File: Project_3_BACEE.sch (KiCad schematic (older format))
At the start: 13 parts, among them U1 DS1337, U2 24LC1025, U3 24LC1025, U4 ATMEGA328P-AU, Y1 Crystal, Y2 Crystal

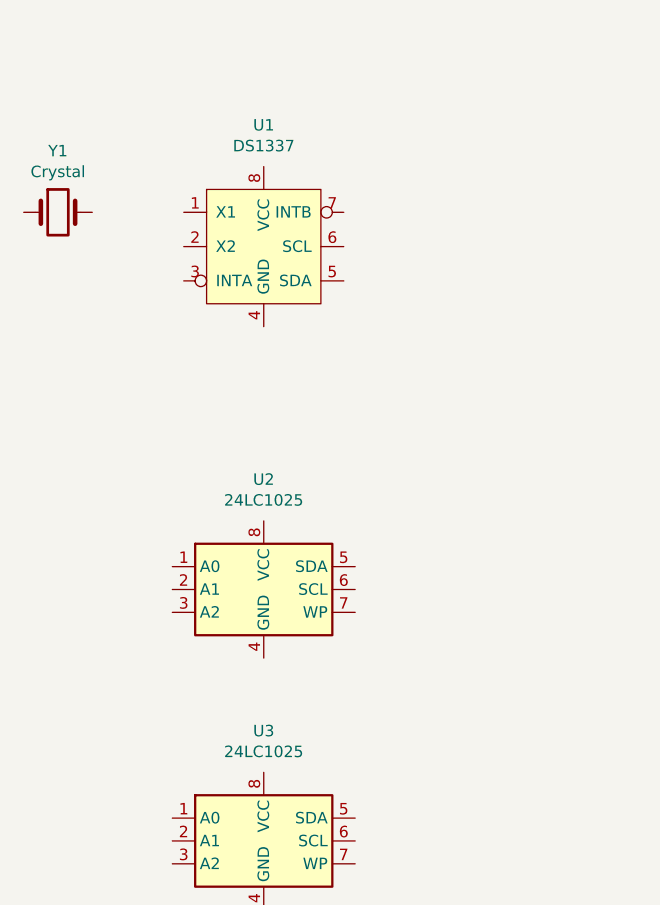
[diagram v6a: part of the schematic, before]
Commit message: Added footprints assigments.
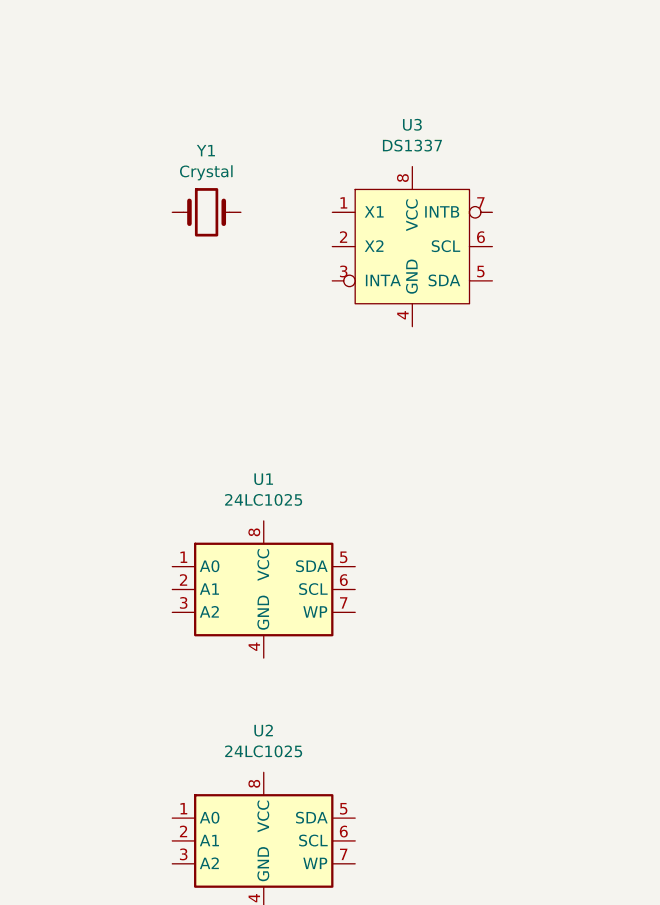
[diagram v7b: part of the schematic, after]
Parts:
- BT1: footprint (none) -> Connector_PinHeader_2.54mm:PinHeader_1x02_P2.54mm_Vertical
- C1, C2, C3: footprint (none) -> Capacitor_SMD:C_0805_2012Metric_Pad1.15x1.40mm_HandSolder
- D1: footprint (none) -> LED_SMD:LED_0805_2012Metric_Pad1.15x1.40mm_HandSolder
- R1, R2: footprint (none) -> Resistor_SMD:R_0805_2012Metric_Pad1.15x1.40mm_HandSolder
- U1: renamed from U2; footprint (none) -> Package_SO:SOIJ-8_5.3x5.3mm_P1.27mm
- U2: renamed from U3; footprint (none) -> Package_SO:SOIJ-8_5.3x5.3mm_P1.27mm
- U3: renamed from U1; footprint (none) -> Package_SO:SO-8_5.3x6.2mm_P1.27mm
- Y1: footprint (none) -> Crystal:Crystal_SMD_MicroCrystal_CC7V-T1A-2Pin_3.2x1.5mm_HandSoldering
- Y2: footprint (none) -> Crystal:Crystal_SMD_5032-2Pin_5.0x3.2mm_HandSoldering
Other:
- moved on the sheet: U3, Y1
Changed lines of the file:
@@
 F 0 "BT1" H 10258 1846 50  0000 L CNN
 F 1 "Battery" H 10258 1755 50  0000 L CNN
-F 2 "" V 10150 1860 50  0001 C CNN
+F 2 "Connector_PinHeader_2.54mm:PinHeader_1x02_P2.54mm_Vertical" V 10150 1860 50  0001 C CNN
 F 3 "~" V 10150 1860 50  0001 C CNN
 	1    10150 1800
@@
 F 0 "C1" H 5215 2696 50  0000 L CNN
 F 1 "C" H 5215 2605 50  0000 L CNN
-F 2 "" H 5138 2500 50  0001 C CNN
+F 2 "Capacitor_SMD:C_0805_2012Metric_Pad1.15x1.40mm_HandSolder" H 5138 2500 50  0001 C CNN
 F 3 "~" H 5100 2650 50  0001 C CNN
 	1    5100 2650
@@
 F 0 "C2" H 5215 3096 50  0000 L CNN
 F 1 "C" H 5215 3005 50  0000 L CNN
-F 2 "" H 5138 2900 50  0001 C CNN
+F 2 "Capacitor_SMD:C_0805_2012Metric_Pad1.15x1.40mm_HandSolder" H 5138 2900 50  0001 C CNN
 F 3 "~" H 5100 3050 50  0001 C CNN
 	1    5100 3050
@@
 F 0 "C3" H 10568 2446 50  0000 L CNN
 F 1 "CP" H 10568 2355 50  0000 L CNN
-F 2 "" H 10488 2250 50  0001 C CNN
+F 2 "Capacitor_SMD:C_0805_2012Metric_Pad1.15x1.40mm_HandSolder" H 10488 2250 50  0001 C CNN
 F 3 "~" H 10450 2400 50  0001 C CNN
 	1    10450 2400
@@
 F 0 "D1" V 4439 4483 50  0000 R CNN
 F 1 "LED" V 4348 4483 50  0000 R CNN
-F 2 "" H 4400 4600 50  0001 C CNN
+F 2 "LED_SMD:LED_0805_2012Metric_Pad1.15x1.40mm_HandSolder" H 4400 4600 50  0001 C CNN
 F 3 "~" H 4400 4600 50  0001 C CNN
 	1    4400 4600
@@
 F 0 "R1" H 4420 2646 50  0000 L CNN
 F 1 "R" H 4420 2555 50  0000 L CNN
-F 2 "" V 4280 2600 50  0001 C CNN
+F 2 "Resistor_SMD:R_0805_2012Metric_Pad1.15x1.40mm_HandSolder" V 4280 2600 50  0001 C CNN
 F 3 "~" H 4350 2600 50  0001 C CNN
 	1    4350 2600
@@
 F 0 "R2" H 4470 4046 50  0000 L CNN
 F 1 "R" H 4470 3955 50  0000 L CNN
-F 2 "" V 4330 4000 50  0001 C CNN
+F 2 "Resistor_SMD:R_0805_2012Metric_Pad1.15x1.40mm_HandSolder" V 4330 4000 50  0001 C CNN
 F 3 "~" H 4400 4000 50  0001 C CNN
 	1    4400 4000
@@
 $EndComp
 $Comp
-L Memory_EEPROM:24LC1025 U2
+L Memory_EEPROM:24LC1025 U1
 U 1 1 5D83A291
 P 2000 4100
-F 0 "U2" H 2000 4581 50  0000 C CNN
+F 0 "U1" H 2000 4581 50  0000 C CNN
 F 1 "24LC1025" H 2000 4490 50  0000 C CNN
-F 2 "" H 2000 4100 50  0001 C CNN
+F 2 "Package_SO:SOIJ-8_5.3x5.3mm_P1.27mm" H 2000 4100 50  0001 C CNN
 F 3 "http://ww1.microchip.com/downloads/en/DeviceDoc/21941B.pdf" H 2000 4100 50  0001 C CNN
 	1    2000 4100
@@
 $EndComp
 $Comp
-L Real_Time_Clock:DS1337 U1
+L Real_Time_Clock:DS1337 U3
 U 1 1 5D83D55D
-P 2000 2600
-F 0 "U1" H 2000 3131 50  0000 C CNN
-F 1 "DS1337" H 2000 3040 50  0000 C CNN
-F 2 "" H 2250 3350 50  0001 C CNN
-F 3 "http://www.farnell.com/datasheets/2000844.pdf?_ga=2.177508589.917776798.1568905288-909876714.1550950510&_gac=1.216414692.1568905288.Cj0KCQjwzozsBRCNARIsAEM9kBOgoySVZbm8O6iFhnJvaEFTPgnKihPjdqZAtUZmWq1n3gbdbDGyVXUaAgFCEALw_wcB" H 2250 3350 50  0001 C CNN
-	1    2000 2600
+P 2650 2600
+F 0 "U3" H 2650 3131 50  0000 C CNN
+F 1 "DS1337" H 2650 3040 50  0000 C CNN
+F 2 "Package_SO:SO-8_5.3x6.2mm_P1.27mm" H 2900 3350 50  0001 C CNN
+F 3 "http://www.farnell.com/datasheets/2000844.pdf?_ga=2.177508589.917776798.1568905288-909876714.1550950510&_gac=1.216414692.1568905288.Cj0KCQjwzozsBRCNARIsAEM9kBOgoySVZbm8O6iFhnJvaEFTPgnKihPjdqZAtUZmWq1n3gbdbDGyVXUaAgFCEALw_wcB" H 2900 3350 50  0001 C CNN
+	1    2650 2600
 	1    0    0    -1
 $EndComp
@@
 L Device:Crystal Y1
 U 1 1 5D83E063
-P 1100 2450
-F 0 "Y1" H 1100 2718 50  0000 C CNN
-F 1 "Crystal" H 1100 2627 50  0000 C CNN
-F 2 "" H 1100 2450 50  0001 C CNN
-F 3 "~" H 1100 2450 50  0001 C CNN
-	1    1100 2450
+P 1750 2450
+F 0 "Y1" H 1750 2718 50  0000 C CNN
+F 1 "Crystal" H 1750 2627 50  0000 C CNN
+F 2 "Crystal:Crystal_SMD_MicroCrystal_CC7V-T1A-2Pin_3.2x1.5mm_HandSoldering" H 1750 2450 50  0001 C CNN
+F 3 "~" H 1750 2450 50  0001 C CNN
+	1    1750 2450
 	1    0    0    -1
 $EndComp
@@
 F 0 "Y2" H 4750 3068 50  0000 C CNN
 F 1 "Crystal" H 4750 2977 50  0000 C CNN
-F 2 "" H 4750 2800 50  0001 C CNN
+F 2 "Crystal:Crystal_SMD_5032-2Pin_5.0x3.2mm_HandSoldering" H 4750 2800 50  0001 C CNN
 F 3 "~" H 4750 2800 50  0001 C CNN
 	1    4750 2800
@@
 $EndComp
 $Comp
-L Memory_EEPROM:24LC1025 U3
+L Memory_EEPROM:24LC1025 U2
 U 1 1 5D841166
 P 2000 5200
-F 0 "U3" H 2000 5681 50  0000 C CNN
+F 0 "U2" H 2000 5681 50  0000 C CNN
 F 1 "24LC1025" H 2000 5590 50  0000 C CNN
-F 2 "" H 2000 5200 50  0001 C CNN
+F 2 "Package_SO:SOIJ-8_5.3x5.3mm_P1.27mm" H 2000 5200 50  0001 C CNN
 F 3 "http://ww1.microchip.com/downloads/en/DeviceDoc/21941B.pdf" H 2000 5200 50  0001 C CNN
 	1    2000 5200

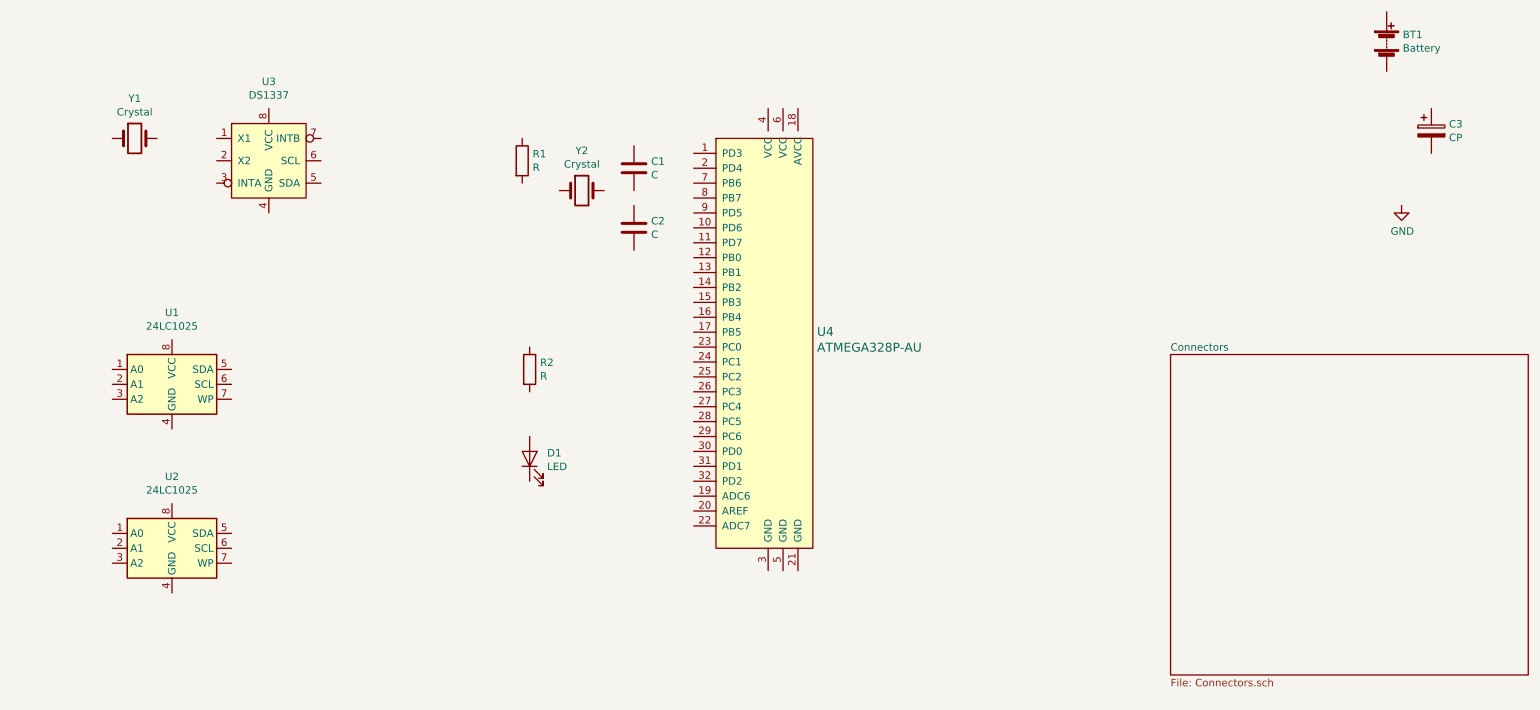
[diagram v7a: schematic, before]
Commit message: Completed asociations and added component values.
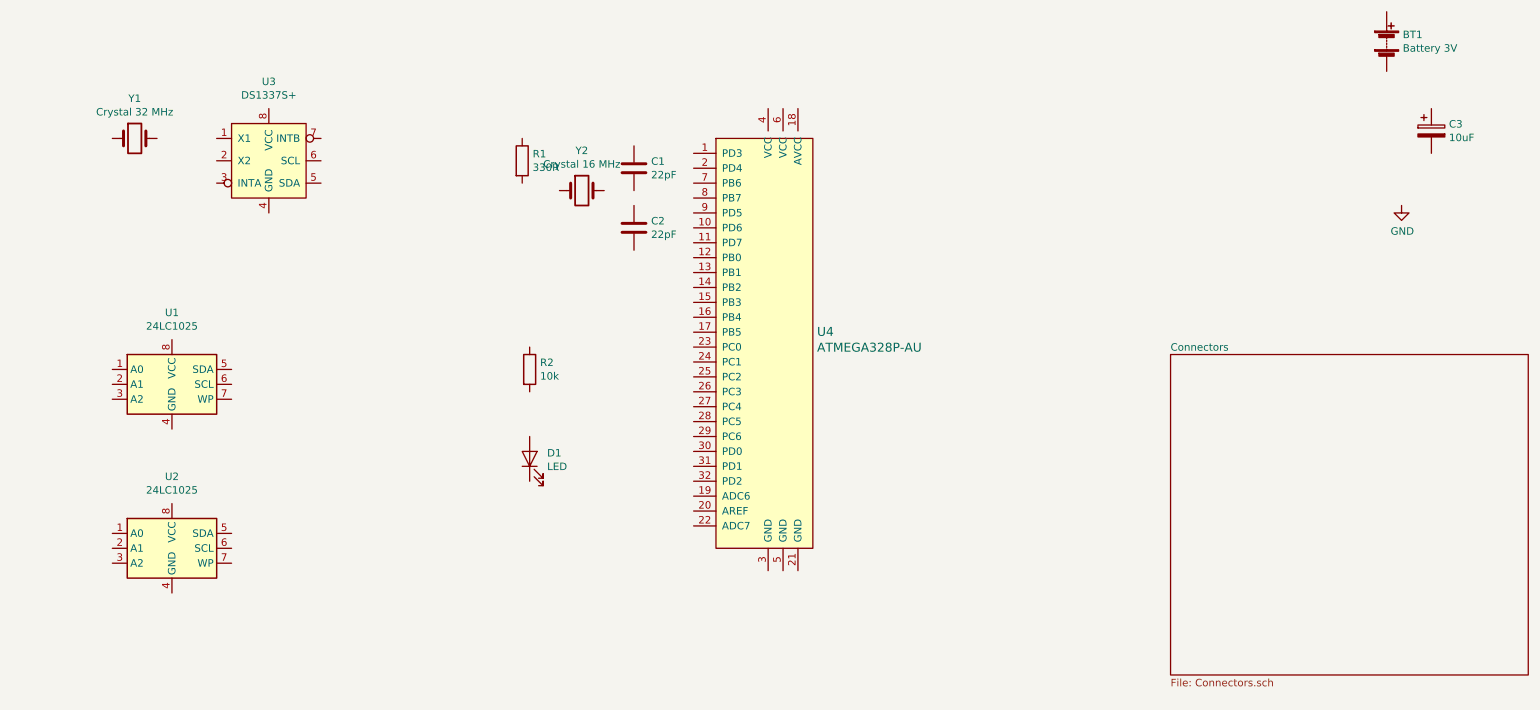
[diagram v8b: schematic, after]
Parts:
- BT1: value Battery -> Battery 3V
- C1, C2: value C -> 22pF
- C3: value CP -> 10uF
- R1: value R -> 330R
- R2: value R -> 10k
- U3: value DS1337 -> DS1337S+
- Y1: value Crystal -> Crystal 32 MHz
- Y2: value Crystal -> Crystal 16 MHz
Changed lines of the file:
@@
 P 10150 1800
 F 0 "BT1" H 10258 1846 50  0000 L CNN
-F 1 "Battery" H 10258 1755 50  0000 L CNN
+F 1 "Battery 3V" H 10258 1755 50  0000 L CNN
 F 2 "Connector_PinHeader_2.54mm:PinHeader_1x02_P2.54mm_Vertical" V 10150 1860 50  0001 C CNN
 F 3 "~" V 10150 1860 50  0001 C CNN
@@
 P 5100 2650
 F 0 "C1" H 5215 2696 50  0000 L CNN
-F 1 "C" H 5215 2605 50  0000 L CNN
+F 1 "22pF" H 5215 2605 50  0000 L CNN
 F 2 "Capacitor_SMD:C_0805_2012Metric_Pad1.15x1.40mm_HandSolder" H 5138 2500 50  0001 C CNN
 F 3 "~" H 5100 2650 50  0001 C CNN
@@
 P 5100 3050
 F 0 "C2" H 5215 3096 50  0000 L CNN
-F 1 "C" H 5215 3005 50  0000 L CNN
+F 1 "22pF" H 5215 3005 50  0000 L CNN
 F 2 "Capacitor_SMD:C_0805_2012Metric_Pad1.15x1.40mm_HandSolder" H 5138 2900 50  0001 C CNN
 F 3 "~" H 5100 3050 50  0001 C CNN
@@
 P 10450 2400
 F 0 "C3" H 10568 2446 50  0000 L CNN
-F 1 "CP" H 10568 2355 50  0000 L CNN
+F 1 "10uF" H 10568 2355 50  0000 L CNN
 F 2 "Capacitor_SMD:C_0805_2012Metric_Pad1.15x1.40mm_HandSolder" H 10488 2250 50  0001 C CNN
 F 3 "~" H 10450 2400 50  0001 C CNN
@@
 P 4350 2600
 F 0 "R1" H 4420 2646 50  0000 L CNN
-F 1 "R" H 4420 2555 50  0000 L CNN
+F 1 "330R" H 4420 2555 50  0000 L CNN
 F 2 "Resistor_SMD:R_0805_2012Metric_Pad1.15x1.40mm_HandSolder" V 4280 2600 50  0001 C CNN
 F 3 "~" H 4350 2600 50  0001 C CNN
@@
 P 4400 4000
 F 0 "R2" H 4470 4046 50  0000 L CNN
-F 1 "R" H 4470 3955 50  0000 L CNN
+F 1 "10k" H 4470 3955 50  0000 L CNN
 F 2 "Resistor_SMD:R_0805_2012Metric_Pad1.15x1.40mm_HandSolder" V 4330 4000 50  0001 C CNN
 F 3 "~" H 4400 4000 50  0001 C CNN
@@
 P 2650 2600
 F 0 "U3" H 2650 3131 50  0000 C CNN
-F 1 "DS1337" H 2650 3040 50  0000 C CNN
+F 1 "DS1337S+" H 2650 3040 50  0000 C CNN
 F 2 "Package_SO:SO-8_5.3x6.2mm_P1.27mm" H 2900 3350 50  0001 C CNN
 F 3 "http://www.farnell.com/datasheets/2000844.pdf?_ga=2.177508589.917776798.1568905288-909876714.1550950510&_gac=1.216414692.1568905288.Cj0KCQjwzozsBRCNARIsAEM9kBOgoySVZbm8O6iFhnJvaEFTPgnKihPjdqZAtUZmWq1n3gbdbDGyVXUaAgFCEALw_wcB" H 2900 3350 50  0001 C CNN
@@
 P 1750 2450
 F 0 "Y1" H 1750 2718 50  0000 C CNN
-F 1 "Crystal" H 1750 2627 50  0000 C CNN
+F 1 "Crystal 32 MHz" H 1750 2627 50  0000 C CNN
 F 2 "Crystal:Crystal_SMD_MicroCrystal_CC7V-T1A-2Pin_3.2x1.5mm_HandSoldering" H 1750 2450 50  0001 C CNN
 F 3 "~" H 1750 2450 50  0001 C CNN
@@
 P 4750 2800
 F 0 "Y2" H 4750 3068 50  0000 C CNN
-F 1 "Crystal" H 4750 2977 50  0000 C CNN
+F 1 "Crystal 16 MHz" H 4750 2977 50  0000 C CNN
 F 2 "Crystal:Crystal_SMD_5032-2Pin_5.0x3.2mm_HandSoldering" H 4750 2800 50  0001 C CNN
 F 3 "~" H 4750 2800 50  0001 C CNN
